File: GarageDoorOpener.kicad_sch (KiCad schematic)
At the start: 30 parts, among them J1 USB_B_Mini, J2 Door Sensor, J3 FTDI, J4 Conn_01x16, J6 Door Switch, Q1 Q_NPN_BEC, SW1 RESET, SW2 FLASH, U1 AMS1117-3.3, U2 ESP32-C3-WROOM-02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

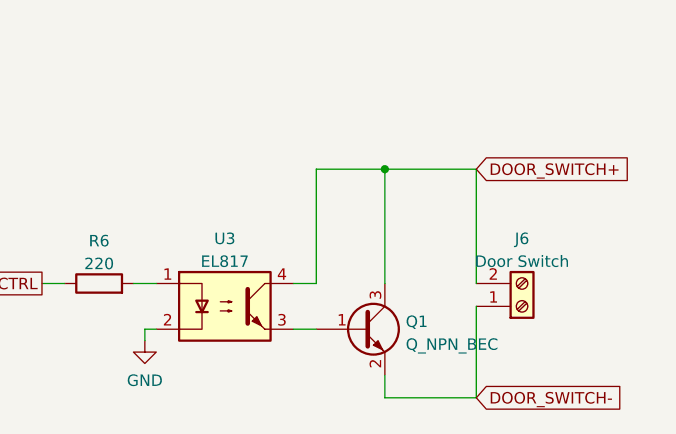
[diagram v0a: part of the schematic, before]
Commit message: Board rev 1.1, add switch capacitor
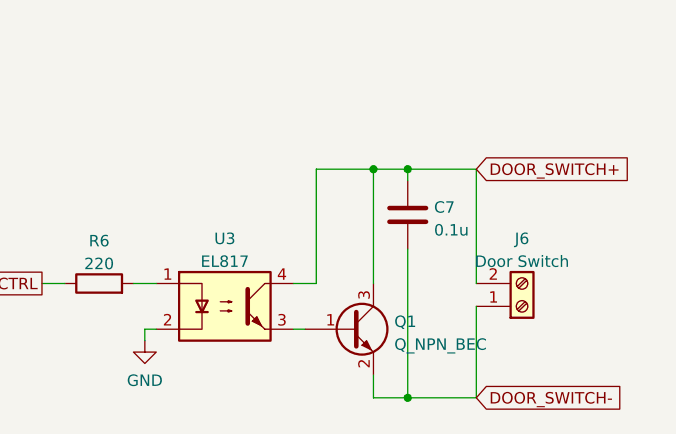
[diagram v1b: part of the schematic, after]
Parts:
- added C7: 0.1u, Capacitor_SMD:C_0805_2012Metric, symbol Device:C
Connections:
- net DOOR_SWITCH+: now also C7.1
- net DOOR_SWITCH-: now also C7.2
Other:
- moved on the sheet: Q1
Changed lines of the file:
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@@
   (paper "USLetter")
   (title_block
-    (rev "1")
+    (rev "1.1")
     (comment 1 "Design for JLCPCB 1-2 Layer Service")
   )
   (junction (at 67.31 96.52) (diameter 0) (color 0 0 0 0)
   )
+  (junction (at 240.03 154.94) (diameter 0) (color 0 0 0 0)
+  )
   (junction (at 107.95 133.35) (diameter 0) (color 0 0 0 0)
   )
   (junction (at 97.79 142.24) (diameter 0) (color 0 0 0 0)
   )
+  (junction (at 240.03 129.54) (diameter 0) (color 0 0 0 0)
+  )
   (junction (at 67.31 105.41) (diameter 0) (color 0 0 0 0)
   )
@@
   (junction (at 52.07 50.8) (diameter 0) (color 0 0 0 0)
   )
-  (junction (at 237.49 129.54) (diameter 0) (color 0 0 0 0)
+  (junction (at 236.22 129.54) (diameter 0) (color 0 0 0 0)
   )
   (no_connect (at 247.65 40.64))
@@
     (stroke (width 0) (type default) (color 0 0 0 0))
   )
-  (wire (pts (xy 237.49 154.94) (xy 247.65 154.94))
+  (wire (pts (xy 236.22 154.94) (xy 240.03 154.94))
     (stroke (width 0) (type default) (color 0 0 0 0))
   )
@@
     (stroke (width 0) (type default) (color 0 0 0 0))
   )
-  (wire (pts (xy 237.49 129.54) (xy 237.49 142.24))
+  (wire (pts (xy 236.22 129.54) (xy 236.22 142.24))
     (stroke (width 0) (type default) (color 0 0 0 0))
   )
@@
     (stroke (width 0) (type default) (color 0 0 0 0))
   )
+  (wire (pts (xy 240.03 129.54) (xy 247.65 129.54))
+    (stroke (width 0) (type default) (color 0 0 0 0))
+  )
   (wire (pts (xy 229.87 33.02) (xy 231.14 33.02))
     (stroke (width 0) (type default) (color 0 0 0 0))
@@
     (stroke (width 0) (type default) (color 0 0 0 0))
   )
-  (wire (pts (xy 229.87 129.54) (xy 237.49 129.54))
-    (stroke (width 0) (type default) (color 0 0 0 0))
-  )
-  (wire (pts (xy 227.33 147.32) (xy 229.87 147.32))
+  (wire (pts (xy 229.87 129.54) (xy 236.22 129.54))
+    (stroke (width 0) (type default) (color 0 0 0 0))
+  )
+  (wire (pts (xy 227.33 147.32) (xy 228.6 147.32))
     (stroke (width 0) (type default) (color 0 0 0 0))
   )
@@
     (stroke (width 0) (type default) (color 0 0 0 0))
   )
+  (wire (pts (xy 240.03 129.54) (xy 240.03 130.81))
+    (stroke (width 0) (type default) (color 0 0 0 0))
+  )
   (wire (pts (xy 72.39 138.43) (xy 71.12 138.43))
     (stroke (width 0) (type default) (color 0 0 0 0))
@@
     (stroke (width 0) (type default) (color 0 0 0 0))
   )
+  (wire (pts (xy 240.03 138.43) (xy 240.03 154.94))
+    (stroke (width 0) (type default) (color 0 0 0 0))
+  )
   (wire (pts (xy 58.42 96.52) (xy 67.31 96.52))
     (stroke (width 0) (type default) (color 0 0 0 0))
@@
     (stroke (width 0) (type default) (color 0 0 0 0))
   )
-  (wire (pts (xy 237.49 129.54) (xy 247.65 129.54))
+  (wire (pts (xy 236.22 129.54) (xy 240.03 129.54))
     (stroke (width 0) (type default) (color 0 0 0 0))
   )
@@
     (stroke (width 0) (type default) (color 0 0 0 0))
   )
+  (wire (pts (xy 240.03 154.94) (xy 247.65 154.94))
+    (stroke (width 0) (type default) (color 0 0 0 0))
+  )
   (wire (pts (xy 67.31 55.88) (xy 69.85 55.88))
     (stroke (width 0) (type default) (color 0 0 0 0))
@@
     (stroke (width 0) (type default) (color 0 0 0 0))
   )
-  (wire (pts (xy 237.49 152.4) (xy 237.49 154.94))
+  (wire (pts (xy 236.22 152.4) (xy 236.22 154.94))
     (stroke (width 0) (type default) (color 0 0 0 0))
   )
@@
     (pin "1")
   )
-  (symbol (lib_id "Device:Q_NPN_BEC") (at 234.95 147.32 0) (unit 1)
-    (in_bom yes) (on_board yes) (fields_autoplaced)
-    (property "Reference" "Q1" (id 0) (at 239.8014 146.4853 0)
-      (effects (font (size 1.27 1.27)) (justify left))
-    )
-    (property "Value" "Q_NPN_BEC" (id 1) (at 239.8014 149.0222 0)
-      (effects (font (size 1.27 1.27)) (justify left))
-    )
-    (property "Footprint" "Package_TO_SOT_SMD:SOT-23" (id 2) (at 240.03 144.78 0)
-      (effects (font (size 1.27 1.27)) hide)
-    )
-    (property "Datasheet" "~" (id 3) (at 234.95 147.32 0)
+  (symbol (lib_id "Device:Q_NPN_BEC") (at 233.68 147.32 0) (unit 1)
+    (in_bom yes) (on_board yes) (fields_autoplaced)
+    (property "Reference" "Q1" (id 0) (at 238.5314 146.4853 0)
+      (effects (font (size 1.27 1.27)) (justify left))
+    )
+    (property "Value" "Q_NPN_BEC" (id 1) (at 238.5314 149.0222 0)
+      (effects (font (size 1.27 1.27)) (justify left))
+    )
+    (property "Footprint" "Package_TO_SOT_SMD:SOT-23" (id 2) (at 238.76 144.78 0)
+      (effects (font (size 1.27 1.27)) hide)
+    )
+    (property "Datasheet" "~" (id 3) (at 233.68 147.32 0)
       (effects (font (size 1.27 1.27)) hide)
     )
@@
     )
     (pin "1")
+  )
+  (symbol (lib_id "Device:C") (at 240.03 134.62 0) (unit 1)
+    (in_bom yes) (on_board yes) (fields_autoplaced)
+    (property "Reference" "C7" (id 0) (at 242.951 133.7853 0)
+      (effects (font (size 1.27 1.27)) (justify left))
+    )
+    (property "Value" "0.1u" (id 1) (at 242.951 136.3222 0)
+      (effects (font (size 1.27 1.27)) (justify left))
+    )
+    (property "Footprint" "Capacitor_SMD:C_0805_2012Metric" (id 2) (at 240.9952 138.43 0)
+      (effects (font (size 1.27 1.27)) hide)
+    )
+    (property "Datasheet" "~" (id 3) (at 240.03 134.62 0)
+      (effects (font (size 1.27 1.27)) hide)
+    )
+    (pin "1")
+    (pin "2")
   )
   (symbol (lib_id "Connector_Generic:Conn_01x06") (at 252.73 33.02 0) (unit 1)
@@
       (reference "C6") (unit 1) (value "1u") (footprint "Capacitor_SMD:C_0805_2012Metric")
     )
+    (path "/ae0a85fb-126b-4e06-a0cc-7b311a4b00c6"
+      (reference "C7") (unit 1) (value "0.1u") (footprint "Capacitor_SMD:C_0805_2012Metric")
+    )
     (path "/3c256f1a-7101-4aab-96c4-3db6c7e07efc"
